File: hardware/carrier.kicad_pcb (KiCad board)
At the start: 2 copper layers, 90 x 60 mm, 58 parts, among them J2 Heltec_J2, J3 Heltec_J3, U1 MT3608, U2 TCA9534PWR, U3 MAX98357A

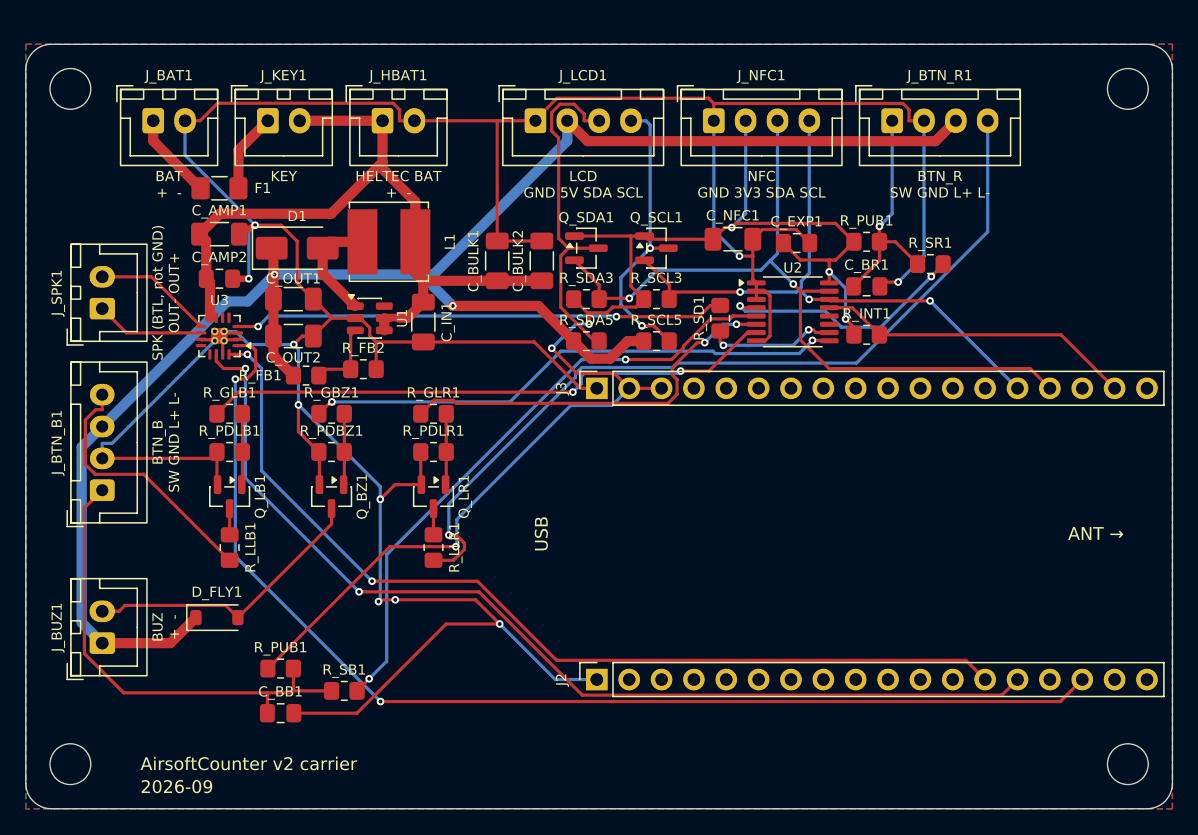
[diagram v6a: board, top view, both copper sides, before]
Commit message: hardware: regenerate for 4-pin XH, add XB8089D cell protection, power model
Regenerated with KiCad 9 after the cloud parts review (make all: ERC 0, DRC 0,
0 unrouted). Six 4-pin XH connectors do not fit the top edge, so J_BTN_R1 moves
to the bottom edge under J2; the schematic connectors shift because Conn_01x04
anchors on pin 2. Two-wire connectors label only pins 1-2 on silk.

The Heltec V4.2 schematic shows no under-voltage cutoff (CN3165 charger, Q4 is
reverse-polarity only), so U4 XB8089D (C79928) goes in the cell negative lead
with R_PROT1 1k / C_PROT1 100nF. Symbol lives in the project lib local.kicad_sym.

power_budget.py estimates runtime per scenario from the Heltec datasheet and
marked estimates (~25 h Deluxe game with backlight, ~40 h without).

Co-Authored-By: Claude Opus 5.5 <noreply@anthropic.com>
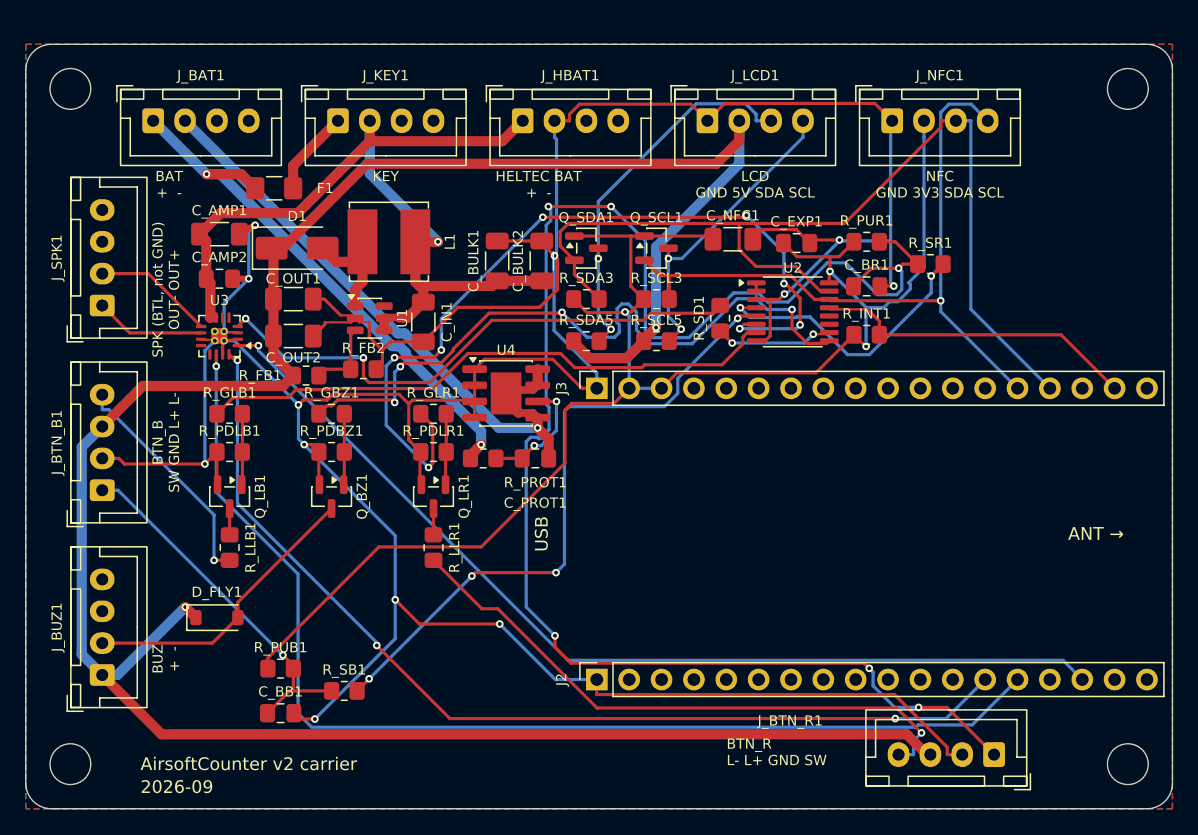
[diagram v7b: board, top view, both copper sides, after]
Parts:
- added C_PROT1: 100nF, Capacitor_SMD:C_0805_2012Metric_Pad1.18x1.45mm_HandSolder, F.Cu at (40.0, 32.5)
- added R_PROT1: 1k, Resistor_SMD:R_0805_2012Metric_Pad1.20x1.40mm_HandSolder, F.Cu at (35.9, 32.5)
- added U4: XB8089D, Package_SO:SOIC-8-1EP_3.9x4.9mm_P1.27mm_EP2.41x3.3mm, F.Cu at (37.7, 27.4)
- J_BAT1, J_BUZ1, J_HBAT1, J_KEY1, J_SPK1: footprint Connector_JST:JST_XH_B2B-XH-A_1x02_P2.50mm_Vertical -> Connector_JST:JST_XH_B4B-XH-A_1x04_P2.50mm_Vertical
- Q_BZ1, Q_LB1, Q_LR1: value AO3400A -> BSS138
- R_GBZ1, R_GLB1, R_GLR1: value 100R -> 1k
- R_PDBZ1, R_PDLB1, R_PDLR1: value 100k -> 10k
- moved J_BTN_R1 50.4 mm to (76.0, 55.8), turned to 180 degrees
- moved J_NFC1 14.0 mm to (68.0, 6.00)
- moved J_LCD1 13.5 mm to (53.5, 6.00)
- moved J_HBAT1 11.0 mm to (39.0, 6.00)
- moved J_KEY1 5.50 mm to (24.5, 6.00)
- moved F1 4.30 mm to (19.5, 11.3)
- moved J_BUZ1 2.50 mm to (6.00, 49.5)
- moved J_SPK1 0.25 mm to (6.00, 20.5)
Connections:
- J_BAT1 pad 2: GND -> BAT_N
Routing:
- net BTN_R_SW: track 18.0 -> 127.4 mm, vias 1 -> 6
- net +5V: track 136.9 -> 194.5 mm
- net BAT_N: track 0.00 -> 48.8 mm, vias 0 -> 1
- net VBAT_RAW: track 6.84 -> 42.7 mm, vias 0 -> 2
- net LED_R_G: track 31.2 -> 65.4 mm, vias 2 -> 8
- net BTN_R_LEDK: track 67.2 -> 47.1 mm
- net SDA_3V3: track 60.3 -> 76.8 mm, vias 2 -> 0
- net I2S_DIN: track 90.8 -> 77.4 mm, vias 2 -> 1
- net +3V3: track 111.2 -> 123.4 mm, vias 6 -> 3
- net BUZ_G: track 42.6 -> 54.2 mm, vias 2 -> 4
- net VBAT_SW: track 59.8 -> 70.7 mm, vias 0 -> 1
- net GND: track 290.7 -> 300.5 mm, vias 10 -> 12
- net I2S_LRCLK: track 79.8 -> 89.3 mm, vias 2 -> 1
- net PROT_VDD: track 0.00 -> 9.44 mm, vias 0 -> 2
- net BTN_B_SW: track 37.5 -> 28.5 mm, vias 0 -> 1
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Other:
- board text added: "BTN_R L- L+ GND SW"
- board text removed: "BTN_R SW GND L+ L-"

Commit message: hardware: replace MAX98357A with NS4168 I2S amp
U3 becomes an NS4168 (C910588, eSOP-8, ~$0.95 cheaper per board, same
Extended setup fee). CTRL high selects the right I2S slot, so firmware must
send audio in the right slot (or both) and hold CTRL low between clips
(13 mA when on). R_SD1 stays in series (CTRL abs max is VDD); new R_SDPD1 10k
on AMP_SD keeps the amp off while the expander floats at reset. C_AMP1 is now
100 uF per the datasheet. Both reuse existing BOM lines.

make all: ERC 0, DRC 0, 0 unrouted. Deluxe 20 BOM lines, Budget 19.

Co-Authored-By: Claude Opus 5.5 <noreply@anthropic.com>
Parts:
- added R_SDPD1: 10k, Resistor_SMD:R_0805_2012Metric_Pad1.20x1.40mm_HandSolder, F.Cu at (75.5, 13.0)
- C_AMP1: value 22uF 25V -> 100uF 6.3V
- U3: value MAX98357A -> NS4168; footprint Package_DFN_QFN:TQFN-16-1EP_3x3mm_P0.5mm_EP1.23x1.23mm_ThermalVias -> Package_SO:HSOP-8-1EP_3.9x4.9mm_P1.27mm_EP2.3x2.3mm_ThermalVias
- moved U3 0.30 mm to (15.2, 23.2), turned to 90 degrees
- turned C_AMP2 to 180 degrees
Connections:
- U3 pad 1: I2S_DIN -> AMP_SD_R
- U3 pad 2: GND -> I2S_LRCLK
- U3 pad 3: GND -> I2S_BCLK
- U3 pad 4: AMP_SD_R -> I2S_DIN
- U3 pad 5: unconnected-(U3-NC-Pad5) -> SPK_N
- U3 pad 6: unconnected-(U3-NC-Pad6) -> VBAT_SW
- U3 pad 7: VBAT_SW -> GND
- U3 pad 8: VBAT_SW -> SPK_P
- U3 pad 9: SPK_P -> GND
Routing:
- net BTN_R_SW: track 127.4 -> 203.5 mm, vias 6 -> 4
- net LED_R_G: track 65.4 -> 29.8 mm, vias 8 -> 2
- net SCL_3V3: track 55.1 -> 85.2 mm
- net AMP_SD_R: track 43.6 -> 71.8 mm, vias 2 -> 4
- net GND: track 300.5 -> 323.4 mm, vias 12 -> 8
- net AMP_SD: track 9.29 -> 30.8 mm, vias 2 -> 3
- net BUZ_K: track 23.1 -> 42.4 mm, vias 0 -> 1
- net BAT_N: track 48.8 -> 64.9 mm
- net +3V3: track 123.4 -> 135.6 mm, vias 3 -> 4
- net +5V: track 194.5 -> 185.0 mm, vias 2 -> 4
- net BUZ_G: track 54.2 -> 45.2 mm
- net SPK_N: track 8.65 -> 15.1 mm, vias 0 -> 1
- net I2S_LRCLK: track 89.3 -> 83.8 mm, vias 1 -> 2
- net SDA_5V: track 30.2 -> 35.6 mm
- net I2S_BCLK: track 79.2 -> 73.8 mm, vias 3 -> 0
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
